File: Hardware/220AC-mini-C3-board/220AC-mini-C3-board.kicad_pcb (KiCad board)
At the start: 2 copper layers, 52.7 x 52.7 mm, 18 parts, among them J1 AC MAINS POWER, J2 ON/OFF switch, J3 Conn_01x04, K1 HF163-F, Q1 Q_NPN_CBE, Q2 Q_NPN_CBE, U1 PBO-3C-3

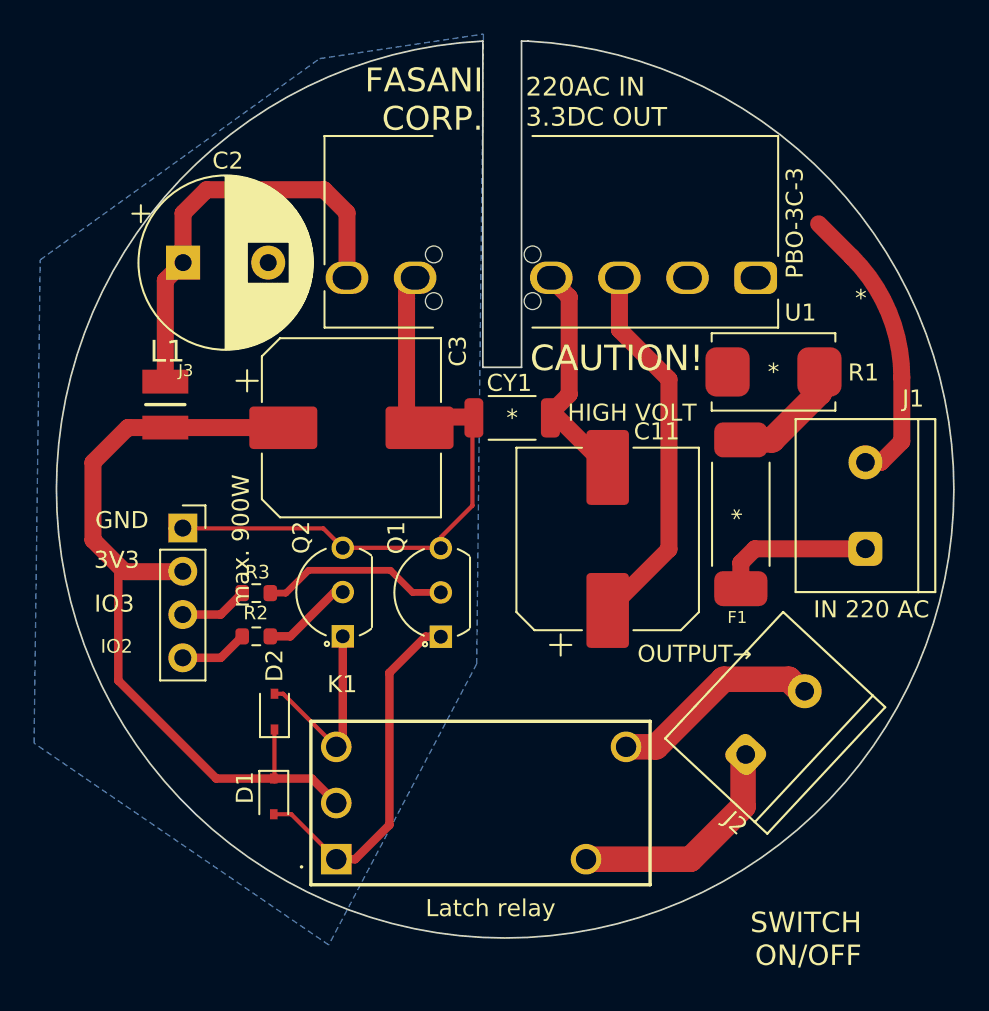
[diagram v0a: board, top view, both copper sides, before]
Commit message: Make CAF refactoring pass schematics
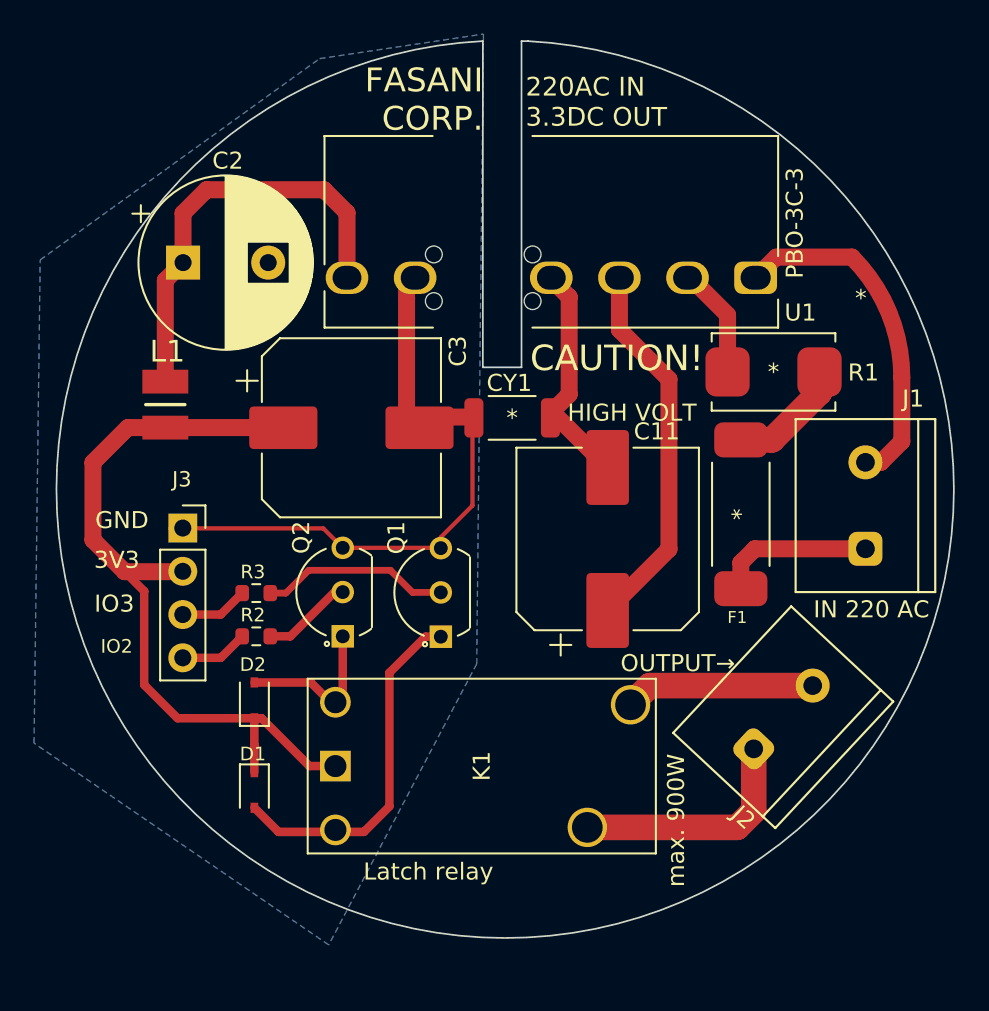
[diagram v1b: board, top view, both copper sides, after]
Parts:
- moved K1 9.06 mm to (126.6, 101.6), turned to 90 degrees
- moved D2 1.35 mm to (121.8, 97.7)
- moved D1 1.20 mm to (121.8, 103.0)
- moved J2 0.57 mm to (152.9, 98.7)
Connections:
- U1 pad 1: Net-(R1-Pad2) -> /AC (N)
- U1 pad 2: /AC (N) -> Net-(R1-Pad2)
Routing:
- net Net-(R1-Pad2): track 0.00 -> 6.60 mm
- net /AC (N): track 17.0 -> 20.4 mm
- net Net-(D2-Pad2): track 11.6 -> 9.16 mm
- net +3V3: track 47.3 -> 45.2 mm
- net Net-(J2-Pad2): track 12.3 -> 11.2 mm
- net Net-(D1-Pad2): track 21.6 -> 20.9 mm
